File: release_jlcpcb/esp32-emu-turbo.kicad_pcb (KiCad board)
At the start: 4 copper layers, 160 x 75 mm, 78 parts, among them J1 USB-C-16P, J3 JST-PH-2P, J4 FPC-40P-0.5mm, SW1 SW-SMD-5.1x5.1, SW10 SW-SMD-5.1x5.1, SW11 SW-SMD-5.1x5.1, SW12 SW-SMD-5.1x5.1, SW13 SW-SMD-5.1x5.1, SW2 SW-SMD-5.1x5.1, SW3 SW-SMD-5.1x5.1, SW4 SW-SMD-5.1x5.1, SW5 SW-SMD-5.1x5.1, SW6 SW-SMD-5.1x5.1, SW7 SW-SMD-5.1x5.1, SW8 SW-SMD-5.1x5.1, SW9 SW-SMD-5.1x5.1, U1 ESP32-S3-WROOM-1-N16R8, U2 ESOP-8, U3 SOT-223, U5 SOP-16, U6 TF-01A

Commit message: fix(pcb): edge clearance, J1 pad gap, power trace widths, PAM8403 thermal vias
5 DFM/review fixes applied:
- Edge clearance: keepout 0.5→0.01mm, CLEARANCE_EDGE 0.50→0.30mm (6→0 segment violations)
- J1 pad clearance: BTN_X channel y=70.60→70.65 (gap 0.10→0.15mm)
- Power trace widths: W_PWR_HIGH=0.76mm for VBUS/BAT+/LX (2.1A paths)
- PAM8403 thermal vias: 3 GND vias within 3-4mm of U5
- Polarity test: SW_RST + SW_BOOT coverage (38/39→40/40)

Verified: DFM 114/114, DFA 9/9, Polarity 40/40. Score: 83→89/100.

Co-Authored-By: Claude Opus 4.6 (1M context) <noreply@anthropic.com>
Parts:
- removed the SPK1 at (30.0, 52.5)
- removed the SW12 at (145.0, 5.50)
- removed the SW3 at (9.00, 32.5)
- removed the SW_PWR at (40.0, 72.0)
- removed the U3 at (125.0, 55.5)
- added C4: C_0805, C_0805, B.Cu at (92.0, 42.0)
- added J3: JST-PH-2P, JST-PH-2P, B.Cu at (80.0, 62.5)
- added J4: FPC-40P-0.5mm, FPC-40P-0.5mm, B.Cu at (135.0, 35.5)
- added L1: SMD-4x4x2, SMD-4x4x2, B.Cu at (110.0, 52.5)
- added LED1: LED_0805, LED_0805, F.Cu at (25.0, 67.5)
- added R12: R_0805, R_0805, B.Cu at (83.0, 46.0)
- added SW_BOOT: SW-SMD-5.1x5.1, SW-SMD-5.1x5.1, B.Cu at (105.0, 65.5)
- SPK1: renamed from J3; value JST-PH-2P -> Speaker-22mm; footprint JST-PH-2P -> Speaker-22mm
- SW12: renamed from J4; value FPC-40P-0.5mm -> SW-SMD-5.1x5.1; footprint FPC-40P-0.5mm -> SW-SMD-5.1x5.1
- SW3: renamed from LED1; value LED_0805 -> SW-SMD-5.1x5.1; footprint LED_0805 -> SW-SMD-5.1x5.1
- SW_PWR: renamed from L1; value SMD-4x4x2 -> SS-12D00G3; footprint SMD-4x4x2 -> SS-12D00G3
- SW_RST: renamed from R12; value R_0805 -> SW-SMD-5.1x5.1; footprint R_0805 -> SW-SMD-5.1x5.1
- U3: renamed from C4; value C_0805 -> SOT-223; footprint C_0805 -> SOT-223
- moved SW_PWR 72.7 mm to (40.0, 72.0)
- moved SPK1 51.0 mm to (30.0, 52.5)
- moved SW3 38.5 mm to (9.00, 32.5)
- moved U3 35.7 mm to (125.0, 55.5)
- moved SW12 31.6 mm to (145.0, 5.50)
- moved SW_RST 22.9 mm to (95.0, 65.5)
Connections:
- SPK1 pad 1: BAT+ -> SPK+
- SPK1 pad 2: GND -> SPK-
- SW12 pad 1: GND -> (no net)
- SW12 pad 2: +3V3 -> GND
- SW12 pad 3: +3V3 -> BTN_R
- SW12 pad 4: GND -> (no net)
- SW3 pad 1: GND -> (no net)
- SW3 pad 2: LED1_RA -> BTN_LEFT
- SW_PWR pad 1: BAT+ -> (no net)
- SW_PWR pad 2: LX -> BAT+
- SW_RST pad 1: (no net) -> EN
- U3 pad 1: +3V3 -> GND
- U3 pad 2: GND -> (no net)
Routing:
- net GND: track 143.6 -> 156.6 mm, vias 63 -> 70
- net BTN_SELECT: track 105.9 -> 109.5 mm, vias 5 -> 6
- net EN: track 0.00 -> 3.65 mm, vias 0 -> 1

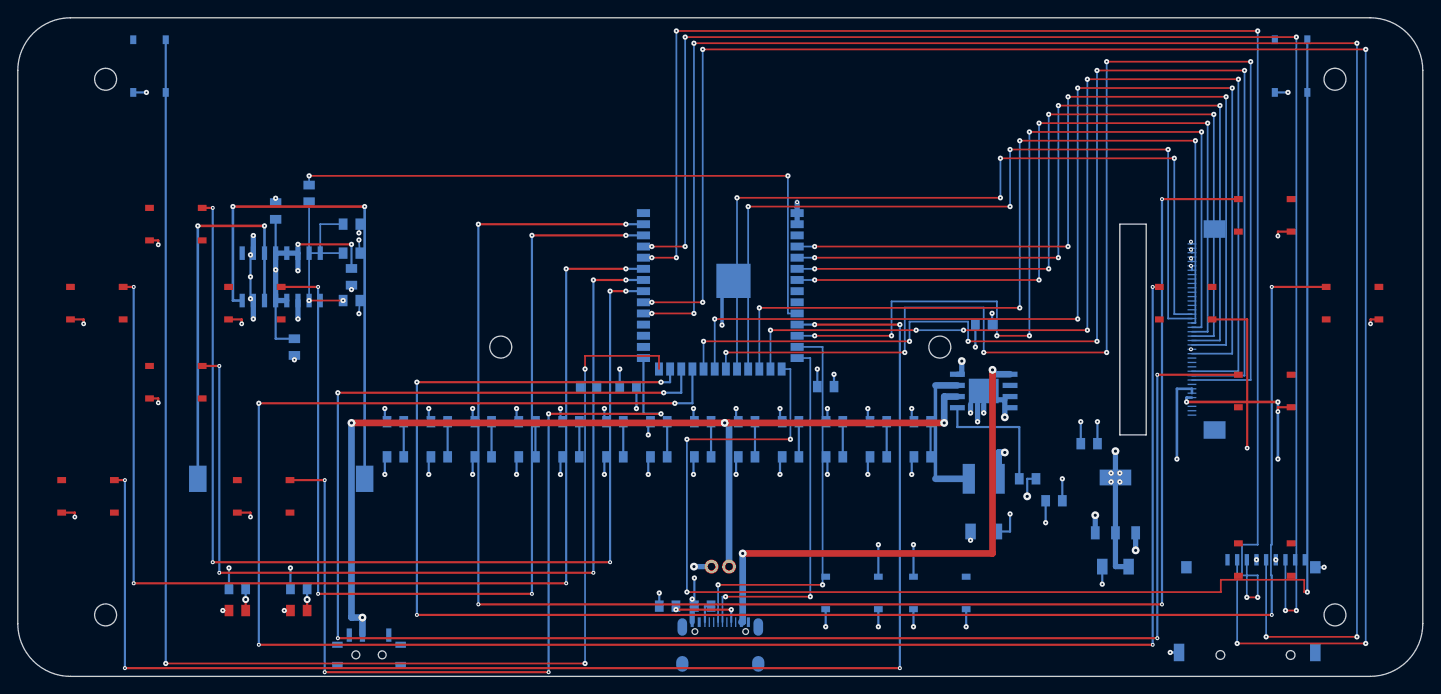
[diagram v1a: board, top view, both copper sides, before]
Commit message: fix(pcb): resolve 22 DFM collisions, add fiducials, GND vias, power stubs
- Fix 22 DFM collision violations (seg-pad, seg-via, via-edge, via-seg, via-via)
- Remove J1 shield pads from F.Cu collision check (SMD B.Cu only, false positives)
- Add 2 board-level fiducials at (12,12) and (148,63)
- Add 3 GND stitching vias near ESP32 and SD card
- Add 2 AMS1117 GND thermal vias for heat dissipation
- Widen VBUS/BAT+ stubs to 0.50-0.76mm, +5V stubs to 0.60mm
- Widen 8 GND B.Cu stubs from 0.3mm to 0.4mm
- Remove incorrect USB D- meander (was on wrong line, worsened mismatch)
- Adjust BTN_START/SELECT/L channel positions for edge/pad clearance
- Shift LCD_CS/DC via positions for segment clearance
- Update PCBA 3D renders and release_jlcpcb package

DFM: 114/114 PASS | Polarity: 40/40 PASS | DFA: 9/9 PASS
Review score: 88/100

Co-Authored-By: Claude Opus 4.6 (1M context) <noreply@anthropic.com>
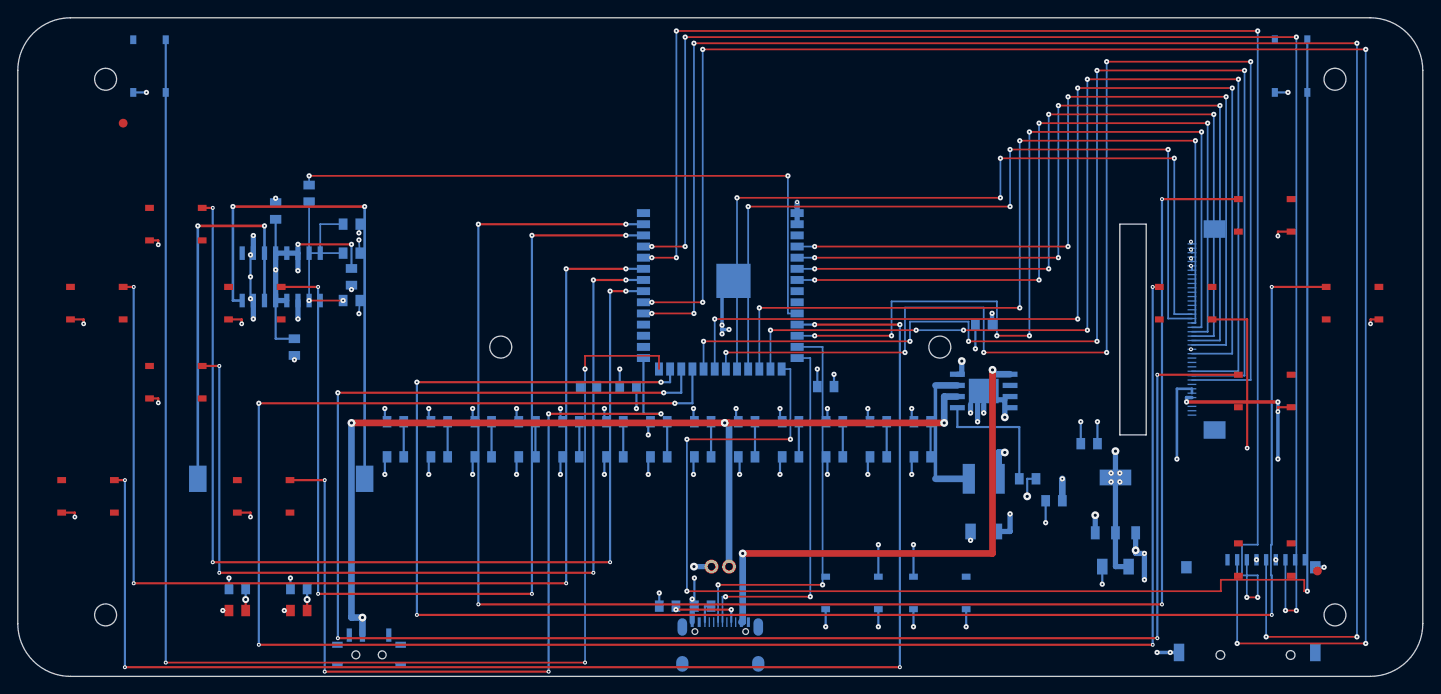
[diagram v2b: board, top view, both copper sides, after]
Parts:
- removed the C3 at (69.5, 42.0)
- removed the C4 at (92.0, 42.0)
- removed the R1 at (74.0, 67.0)
- removed the R2 at (78.0, 67.0)
- removed the R3 at (65.0, 42.0)
- removed the SW8 at (133.0, 32.5)
- removed the SW_BOOT at (105.0, 65.5)
- removed the SW_PWR at (40.0, 72.0)
- added C1: C_0805, C_0805, B.Cu at (122.0, 48.5)
- added C2: C_1206, C_1206, B.Cu at (125.0, 62.5)
- added C21: C_0805, C_0805, B.Cu at (38.0, 23.5)
- added C23: C_0805, C_0805, B.Cu at (38.0, 29.5)
- added C24: C_0805, C_0805, B.Cu at (29.4, 22.0)
- added C25: C_0805, C_0805, B.Cu at (31.5, 37.5)
- added FID1: Fiducial, Fiducial, F.Cu at (12.0, 12.0)
- added FID2: Fiducial, Fiducial, F.Cu at (148.0, 63.0)
- added LED1: LED_0805, LED_0805, F.Cu at (25.0, 67.5)
- added U3: SOT-223, SOT-223, B.Cu at (125.0, 55.5)
- C14: renamed from C19; value C_1206 -> C_0805; footprint C_1206 -> C_0805
- C16: renamed from R20; value R_0805 -> C_0805; footprint R_0805 -> C_0805
- C19: renamed from C24; value C_0805 -> C_1206; footprint C_0805 -> C_1206
- C20: renamed from R21; value R_0805 -> C_0805; footprint R_0805 -> C_0805
- C3: renamed from R6; value R_0805 -> C_0805; footprint R_0805 -> C_0805
- C4: renamed from R7; value R_0805 -> C_0805; footprint R_0805 -> C_0805
- R12: renamed from C5; value C_0805 -> R_0805; footprint C_0805 -> R_0805
- R13: renamed from C6; value C_0805 -> R_0805; footprint C_0805 -> R_0805
- R14: renamed from C7; value C_0805 -> R_0805; footprint C_0805 -> R_0805
- R15: renamed from C8; value C_0805 -> R_0805; footprint C_0805 -> R_0805
- R16: renamed from C10; value C_0805 -> R_0805; footprint C_0805 -> R_0805
- R19: renamed from C9; value C_0805 -> R_0805; footprint C_0805 -> R_0805
- R20: renamed from C1; value C_0805 -> R_0805; footprint C_0805 -> R_0805
- R21: renamed from C2; value C_1206 -> R_0805; footprint C_1206 -> R_0805
- SW8: renamed from LED1; value LED_0805 -> SW-SMD-5.1x5.1; footprint LED_0805 -> SW-SMD-5.1x5.1
- SW_BOOT: renamed from R17; value R_0805 -> SW-SMD-5.1x5.1; footprint R_0805 -> SW-SMD-5.1x5.1
- SW_PWR: renamed from U3; value SOT-223 -> SS-12D00G3; footprint SOT-223 -> SS-12D00G3
- moved SW8 113.5 mm to (133.0, 32.5)
- moved R21 92.1 mm to (38.0, 32.2)
- moved C19 88.5 mm to (110.0, 58.5)
- moved R20 86.8 mm to (38.0, 26.8)
- moved SW_PWR 86.6 mm to (40.0, 72.0)
- moved C18 84.0 mm to (118.0, 55.0)
- moved SW_BOOT 80.0 mm to (105.0, 65.5)
- moved C17 72.9 mm to (110.0, 35.0)
- moved C20 67.4 mm to (103.0, 50.0)
- moved C15 66.9 mm to (93.0, 50.0)
- moved C16 64.3 mm to (98.0, 50.0)
- moved R16 47.1 mm to (115.0, 52.5)
- moved R17 42.5 mm to (25.0, 65.0)
- moved R1 42.0 mm to (74.0, 67.0)
- moved R2 40.8 mm to (78.0, 67.0)
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- renumbered C16 to C10, C20 to C11, C17 to C12, C18 to C13, C22 to C15, C21 to C17, C23 to C18, C25 to C22, C11 to C5, C12 to C6, C13 to C7, C14 to C8, C15 to C9, R18 to R1, R19 to R10, R16 to R11, R8 to R17, R9 to R18, R4 to R2, R5 to R3, R10 to R4, R11 to R5, R12 to R6, R13 to R7, R14 to R8, R15 to R9
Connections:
- C12 pad 1: VBUS -> (no net)
- C12 pad 2: GND -> (no net)
- C13 pad 1: BAT+ -> (no net)
- C13 pad 2: GND -> (no net)
- C14 pad 1: +5V -> (no net)
- C14 pad 2: GND -> (no net)
- C15 pad 1: I2S_DOUT -> (no net)
- C15 pad 2: I2S_DOUT -> (no net)
- C16 pad 1: GND -> (no net)
- C16 pad 2: I2S_DOUT -> (no net)
- C17 pad 1: GND -> VBUS
- C17 pad 2: PAM_VREF -> GND
- C18 pad 1: +5V -> BAT+
- C19 pad 1: GND -> +5V
- C19 pad 2: +5V -> GND
- C20 pad 1: GND -> (no net)
- C20 pad 2: I2S_DOUT -> (no net)
- C22 pad 1: +5V -> I2S_DOUT
- C22 pad 2: GND -> I2S_DOUT
- C3 pad 1: (no net) -> +3V3
- C3 pad 2: (no net) -> GND
- C4 pad 1: (no net) -> +3V3
- C4 pad 2: (no net) -> GND
- R1 pad 1: LED2_RA -> USB_CC1
- R1 pad 2: +3V3 -> GND
- R11 pad 1: +5V -> (no net)
- R11 pad 2: IP5306_KEY -> (no net)
- R16 pad 1: (no net) -> +5V
- R16 pad 2: (no net) -> IP5306_KEY
- R17 pad 1: (no net) -> LED1_RA
- R17 pad 2: (no net) -> +3V3
- R18 pad 1: (no net) -> LED2_RA
- R18 pad 2: (no net) -> +3V3
- R2 pad 1: (no net) -> USB_CC2
- R2 pad 2: (no net) -> GND
- R20 pad 1: +5V -> GND
- R20 pad 2: GND -> I2S_DOUT
- R21 pad 1: +3V3 -> GND
- R21 pad 2: GND -> I2S_DOUT
- SW8 pad 1: GND -> BTN_Y
- SW8 pad 2: LED1_RA -> (no net)
- SW_BOOT pad 1: LED1_RA -> (no net)
- SW_BOOT pad 2: +3V3 -> BTN_SELECT
- SW_PWR pad 1: GND -> (no net)
- SW_PWR pad 2: (no net) -> BAT+
- SW_PWR pad 3: +5V -> (no net)
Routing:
- net GND: track 156.6 -> 164.4 mm, vias 70 -> 75
- net +3V3: track 61.2 -> 58.9 mm

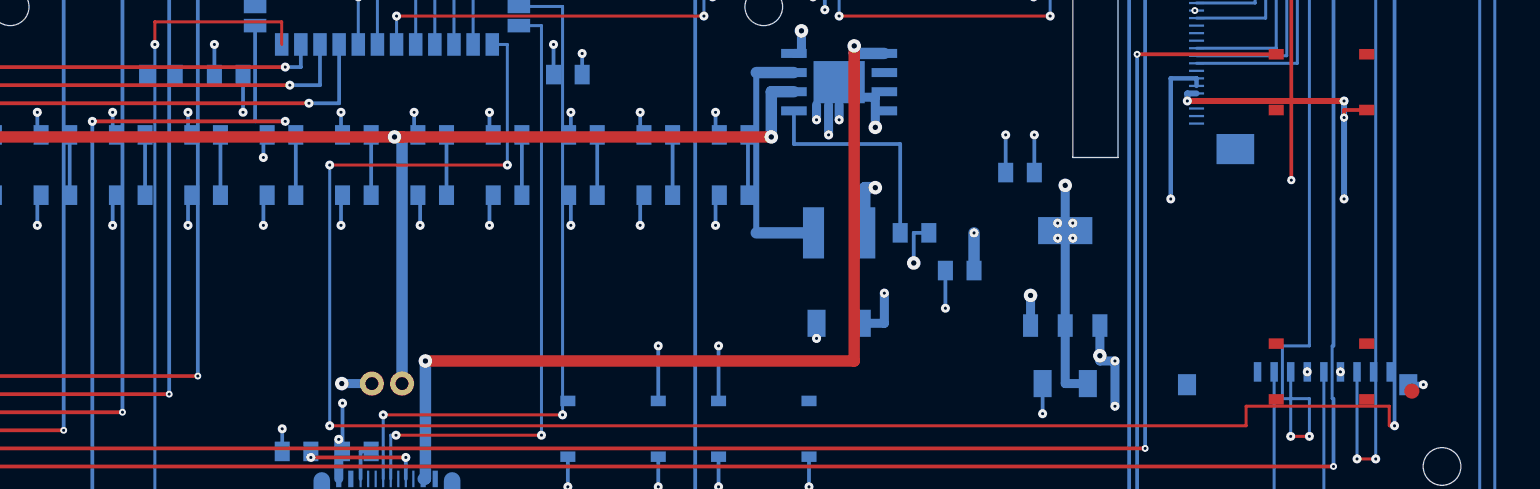
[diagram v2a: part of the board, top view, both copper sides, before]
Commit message: fix(pcb): resolve 3 JLCPCB DFM pad spacing violations
- Fix R10 pad vs pull-up via gap (0.02mm→0.17mm): shrink via to 0.46mm, shift x=73.05
- Fix FID2 fiducial overlap with via: move FID2 from (148,63) to (150,63)
- Fix J4[38] FPC pad vs GND via gap (0.14mm→0.26mm): shift via x=133.10→133.00

DFM: 114/114 PASS | Polarity: 40/40 PASS | DFA: 9/9 PASS

Co-Authored-By: Claude Opus 4.6 (1M context) <noreply@anthropic.com>
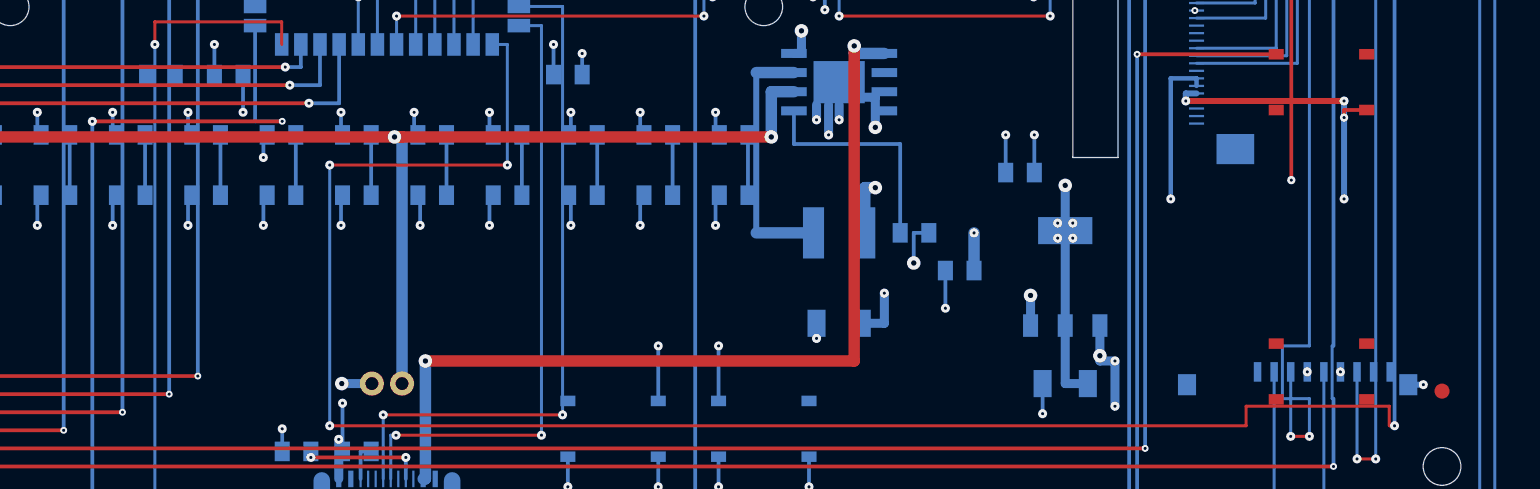
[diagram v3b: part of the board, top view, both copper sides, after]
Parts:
- moved FID2 2.00 mm to (150.0, 63.0)
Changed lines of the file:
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@@
     (pad "1" smd circle (at 0 0) (size 1.0 1.0) (layers "F.Cu" "F.Mask") (net 0 "") (solder_mask_margin 0.5))
   )
-  (footprint "Fiducial" (at 148 63) (layer "F.Cu")
+  (footprint "Fiducial" (at 150 63) (layer "F.Cu")
     (property "Reference" "FID2" (at 0 -2 0) (layer "F.Fab") (effects (font (size 1 1) (thickness 0.2))))
     (property "Value" "Fiducial" (at 0 2 0) (layer "F.Fab") (effects (font (size 1 1) (thickness 0.2))))
@@
   (via (at 133.6 28.25) (size 0.46) (drill 0.2) (layers "F.Cu" "B.Cu") (net 1))
   (segment (start 133.712 28.75) (end 133.712 28.25) (width 0.25) (layer "B.Cu") (net 1))
-  (segment (start 133.712 43.25) (end 133.1 43.25) (width 0.4) (layer "B.Cu") (net 1))
-  (segment (start 133.1 43.25) (end 133.1 43.75) (width 0.4) (layer "B.Cu") (net 1))
-  (via (at 133.1 43.75) (size 0.6) (drill 0.2) (layers "F.Cu" "B.Cu") (net 1))
-  (segment (start 133.1 43.75) (end 143.5 43.75) (width 0.4) (layer "F.Cu") (net 1))
+  (segment (start 133.712 43.25) (end 133.0 43.25) (width 0.4) (layer "B.Cu") (net 1))
+  (segment (start 133.0 43.25) (end 133.0 43.75) (width 0.4) (layer "B.Cu") (net 1))
+  (via (at 133.0 43.75) (size 0.6) (drill 0.2) (layers "F.Cu" "B.Cu") (net 1))
+  (segment (start 133.0 43.75) (end 143.5 43.75) (width 0.4) (layer "F.Cu") (net 1))
   (via (at 143.5 43.75) (size 0.6) (drill 0.2) (layers "F.Cu" "B.Cu") (net 1))
   (segment (start 143.5 43.75) (end 143.5 50.25) (width 0.4) (layer "B.Cu") (net 1))
@@
   (segment (start 60.45 74.46) (end 60.45 45.1) (width 0.25) (layer "B.Cu") (net 36))
   (via (at 60.45 45.1) (size 0.6) (drill 0.2) (layers "F.Cu" "B.Cu") (net 36))
-  (segment (start 60.45 45.1) (end 73.25 45.1) (width 0.25) (layer "F.Cu") (net 36))
-  (via (at 73.25 45.1) (size 0.6) (drill 0.2) (layers "F.Cu" "B.Cu") (net 36))
-  (segment (start 73.25 45.1) (end 71.25 45.1) (width 0.25) (layer "B.Cu") (net 36))
+  (segment (start 60.45 45.1) (end 73.05 45.1) (width 0.25) (layer "F.Cu") (net 36))
+  (via (at 73.05 45.1) (size 0.46) (drill 0.2) (layers "F.Cu" "B.Cu") (net 36))
+  (segment (start 73.05 45.1) (end 71.25 45.1) (width 0.25) (layer "B.Cu") (net 36))
   (segment (start 71.25 45.1) (end 71.25 38.75) (width 0.25) (layer "B.Cu") (net 36))
   (segment (start 25.0 56.35) (end 26.5 56.35) (width 0.25) (layer "F.Cu") (net 1))
